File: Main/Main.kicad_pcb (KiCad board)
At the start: 2 copper layers, 65 x 65 mm, 36 parts, among them J1 Conn_01x03_Pin, J11 Xiao Connector, J2 ToF Sensor, J3 SERVO_PAN, J4 SERVO_TILT, J5 SERVO_GATE, J6 MotorA, J7 MotorB, J8 5VIN, J9 USB_C_Receptacle_USB2.0_16P, U1 ESP32-S3-WROOM-1, U2 Motor Driver, U3 3.3V Reg

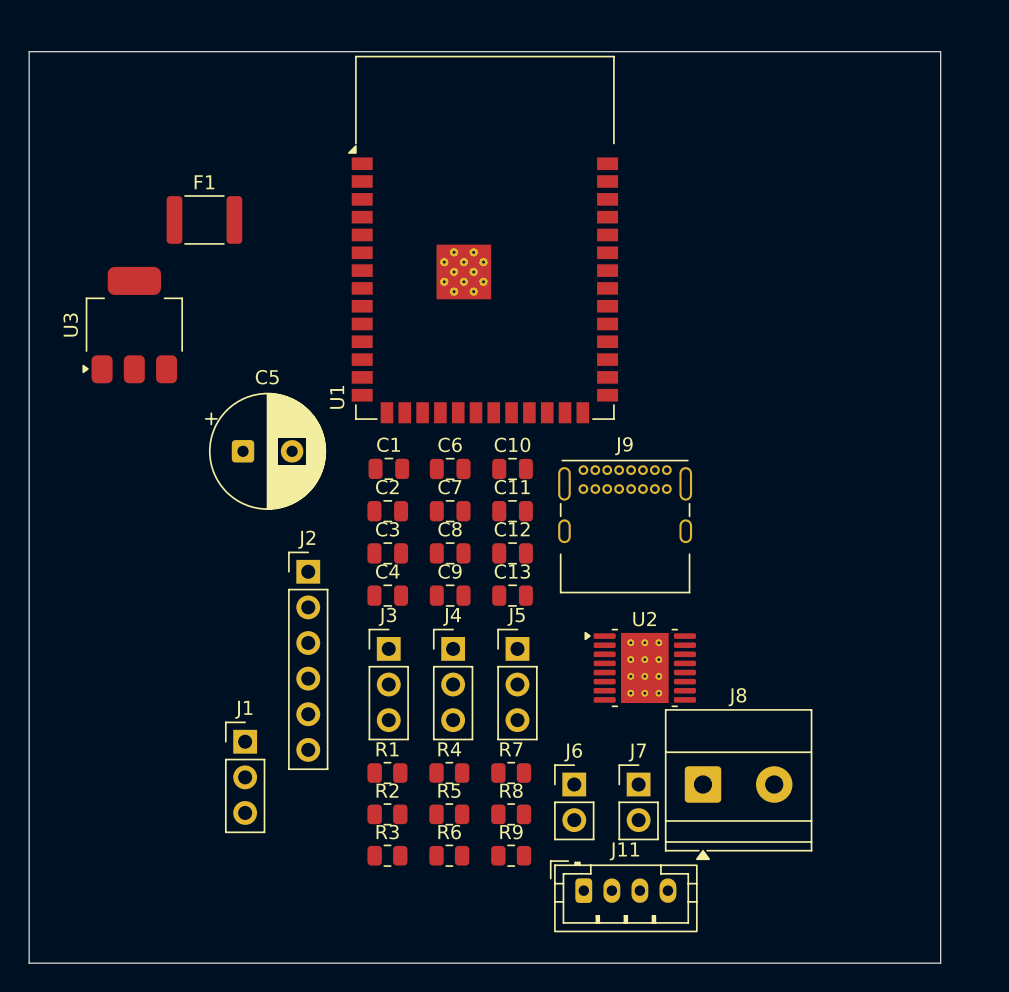
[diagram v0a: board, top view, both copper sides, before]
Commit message: Update net assignments and main board power
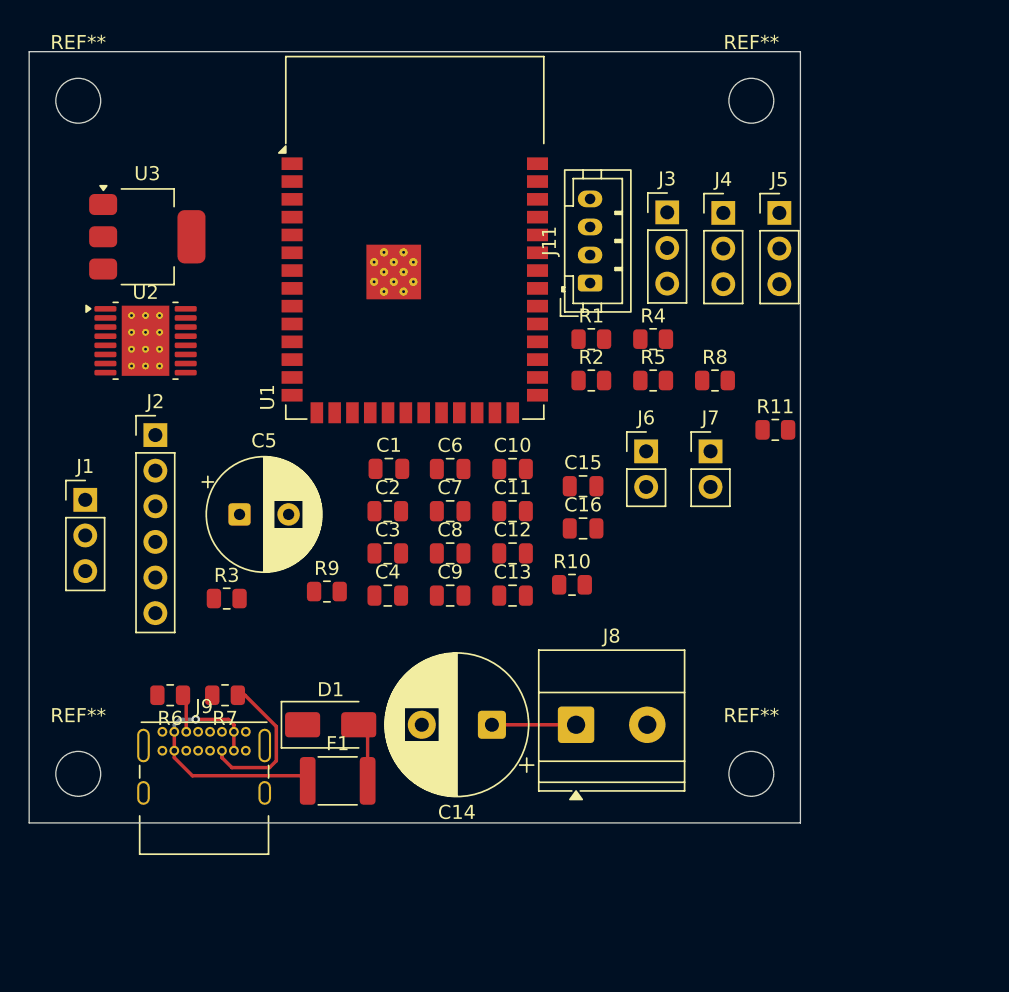
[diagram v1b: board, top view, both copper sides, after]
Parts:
- added C14: 470µF, Capacitor_THT:CP_Radial_D10.0mm_P5.00mm, F.Cu at (45.0, 60.0)
- added C15: 0.1µF, Capacitor_SMD:C_0805_2012Metric, F.Cu at (51.5, 43.0)
- added C16: 0.1µF, Capacitor_SMD:C_0805_2012Metric, F.Cu at (51.5, 46.0)
- added D1: SS34, Diode_SMD:D_SMA, F.Cu at (33.5, 60.0)
- added R10: 10k, Resistor_SMD:R_0805_2012Metric, F.Cu at (50.7, 50.0)
- added R11: 10k, Resistor_SMD:R_0805_2012Metric, F.Cu at (65.2, 39.0)
- added REF**: MountingHole_3.2mm_M3, MountingHole:MountingHole_3.2mm_M3, F.Cu at (15.5, 15.5)
- added REF**: MountingHole_3.2mm_M3, MountingHole:MountingHole_3.2mm_M3, F.Cu at (15.5, 63.5)
- added REF**: MountingHole_3.2mm_M3, MountingHole:MountingHole_3.2mm_M3, F.Cu at (63.5, 15.5)
- added REF**: MountingHole_3.2mm_M3, MountingHole:MountingHole_3.2mm_M3, F.Cu at (63.5, 63.5)
- F1: value 2A hold / ~4A -> 2A hold/~4A
- moved J11 43.3 mm to (52.0, 28.5), turned to 90 degrees
- moved U2 42.6 mm to (20.3, 32.6)
- moved F1 41.1 mm to (34.0, 64.0)
- moved J3 36.9 mm to (57.5, 23.5)
- moved J4 36.6 mm to (61.5, 23.5)
- moved J5 36.3 mm to (65.5, 23.5)
- moved J9 35.3 mm to (21.5, 60.5)
- moved R1 34.2 mm to (52.1, 32.5)
- moved R2 34.2 mm to (52.1, 35.5)
- moved R4 34.2 mm to (56.5, 32.5)
- moved R5 34.2 mm to (56.5, 35.5)
- moved R8 34.2 mm to (60.9, 35.5)
- moved J6 24.3 mm to (56.0, 40.5)
- moved J7 24.3 mm to (60.6, 40.5)
- moved R9 23.0 mm to (33.2, 50.5)
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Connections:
- F1 pad 2: +5V -> Net-(D1-A)
- U1 pad 21: unconnected-(U1-IO13-Pad21) -> FLY_A_TACH
- U1 pad 22: unconnected-(U1-IO14-Pad22) -> FLY_B_TACH
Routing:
- net Net-(F1-Pad1): track 0.00 -> 19.0 mm, vias 0 -> 1
- net Net-(J9-CC2): track 0.00 -> 11.0 mm
- net +5V: track 0.00 -> 6.00 mm
- net Net-(D1-A): track 0.00 -> 4.26 mm
- net Net-(J9-CC1): track 0.00 -> 2.70 mm
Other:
- board size 65 x 65 mm -> 55 x 55 mm

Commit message: Voltage Reg and EN and Boot
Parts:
- moved U3 37.1 mm to (48.0, 50.0)
- moved R5 35.4 mm to (24.2, 50.0), turned to -90 degrees
- moved R4 34.5 mm to (26.8, 50.0), turned to -90 degrees
- moved C11 32.2 mm to (22.3, 23.5)
- moved C15 32.2 mm to (27.3, 21.7)
- moved C2 32.2 mm to (13.4, 23.5)
- moved C3 32.2 mm to (13.4, 26.5)
- moved C4 32.2 mm to (13.4, 29.5)
- moved C6 32.2 mm to (17.8, 20.5)
- moved C7 32.2 mm to (17.8, 23.5)
- moved C8 32.2 mm to (17.8, 26.5)
- moved R10 32.2 mm to (26.5, 28.8)
- moved C1 32.2 mm to (13.4, 20.5)
- moved C12 32.2 mm to (22.3, 26.5)
- moved C16 32.2 mm to (27.3, 24.8)
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- renumbered C14 to C16
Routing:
- net +3V3: track 0.00 -> 27.4 mm
- net +5V: track 6.00 -> 17.4 mm
- net EN: track 0.00 -> 5.88 mm
- net IO0: track 0.00 -> 3.80 mm

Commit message: Motor Driver
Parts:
- moved J2 64.1 mm to (78.4, 26.3)
- moved C5 47.1 mm to (69.3, 39.8)
- moved R2 41.5 mm to (15.5, 55.0), turned to 180 degrees
- moved R1 40.2 mm to (15.5, 49.2)
- moved C2 34.1 mm to (26.6, 55.0), turned to 90 degrees
- moved C1 33.3 mm to (28.8, 50.0), turned to 180 degrees
- moved U2 19.4 mm to (21.2, 52.0)
- moved R9 19.1 mm to (22.8, 31.6)
- moved C13 12.8 mm to (34.4, 52.0)
- moved R4 12.8 mm to (39.4, 52.0)
- moved R5 12.8 mm to (36.9, 52.0)
- moved R3 10.7 mm to (28.7, 52.2), turned to 180 degrees
- moved J1 8.71 mm to (31.1, 55.6)
- moved J6 6.61 mm to (51.8, 35.4)
- moved J7 6.61 mm to (56.4, 35.4)
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- renumbered C16 to C17
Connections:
- net USB_D− renamed USB_D-
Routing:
- net +5V: track 17.4 -> 49.6 mm
- net DRV_SLEEP: track 0.00 -> 31.3 mm, vias 0 -> 2
- net +3V3: track 27.4 -> 52.3 mm
- net VM: track 0.00 -> 5.65 mm
- net Net-(U2-VCP): track 0.00 -> 4.62 mm
- net Net-(U2-VINT): track 0.00 -> 4.21 mm
- net IO0: track 3.80 -> 6.91 mm
- net DRV_FAULT: track 0.00 -> 2.23 mm
- net Net-(D1-A): track 4.26 -> 6.29 mm
- net EN: track 5.88 -> 6.95 mm
